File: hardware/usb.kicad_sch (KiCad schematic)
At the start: 6 parts, among them J601 USB_C_Receptacle_USB2.0, U601 SRV05-4

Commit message: work on layout
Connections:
- net USB_M: now also C?.1, U601.3 (IO2); no longer C?.1, U601.1 (IO1)
- net USB_P: now also C?.1, U601.1 (IO1); no longer C?.1, U601.3 (IO2)
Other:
- moved on the sheet: JP601, R601, U601
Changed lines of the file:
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@@
     (company "matei repair lab")
   )
-  (junction (at 170.18 93.98) (diameter 0) (color 0 0 0 0)
-  )
-  (junction (at 190.5 74.93) (diameter 0) (color 0 0 0 0)
+  (junction (at 160.02 88.9) (diameter 0) (color 0 0 0 0)
+  )
+  (junction (at 182.88 74.93) (diameter 0) (color 0 0 0 0)
   )
   (junction (at 149.86 88.9) (diameter 0) (color 0 0 0 0)
@@
   (junction (at 133.35 88.9) (diameter 0) (color 0 0 0 0)
   )
-  (junction (at 190.5 115.57) (diameter 0) (color 0 0 0 0)
+  (junction (at 182.88 115.57) (diameter 0) (color 0 0 0 0)
   )
   (junction (at 133.35 87.63) (diameter 0) (color 0 0 0 0)
@@
   (junction (at 133.35 93.98) (diameter 0) (color 0 0 0 0)
   )
-  (no_connect (at 203.2 93.98))
+  (no_connect (at 195.58 93.98))
   (no_connect (at 129.54 105.41))
-  (no_connect (at 203.2 88.9))
+  (no_connect (at 195.58 88.9))
   (no_connect (at 129.54 102.87))
-  (wire (pts (xy 170.18 86.36) (xy 170.18 93.98))
-    (stroke (width 0) (type default))
-  )
-  (wire (pts (xy 190.5 115.57) (xy 190.5 104.14))
+  (wire (pts (xy 182.88 115.57) (xy 182.88 104.14))
+    (stroke (width 0) (type default))
+  )
+  (wire (pts (xy 160.02 86.36) (xy 160.02 88.9))
     (stroke (width 0) (type default))
   )
@@
     (stroke (width 0) (type default))
   )
-  (wire (pts (xy 190.5 74.93) (xy 190.5 78.74))
-    (stroke (width 0) (type default))
-  )
-  (wire (pts (xy 190.5 115.57) (xy 190.5 118.11))
+  (wire (pts (xy 182.88 74.93) (xy 182.88 78.74))
+    (stroke (width 0) (type default))
+  )
+  (wire (pts (xy 182.88 115.57) (xy 182.88 118.11))
     (stroke (width 0) (type default))
   )
@@
     (stroke (width 0) (type default))
   )
-  (wire (pts (xy 190.5 74.93) (xy 190.5 72.39))
-    (stroke (width 0) (type default))
-  )
-  (wire (pts (xy 170.18 93.98) (xy 177.8 93.98))
+  (wire (pts (xy 182.88 74.93) (xy 182.88 72.39))
     (stroke (width 0) (type default))
   )
@@
     (stroke (width 0) (type default))
   )
-  (wire (pts (xy 114.3 115.57) (xy 190.5 115.57))
-    (stroke (width 0) (type default))
-  )
-  (wire (pts (xy 149.86 88.9) (xy 177.8 88.9))
-    (stroke (width 0) (type default))
-  )
-  (wire (pts (xy 129.54 74.93) (xy 179.07 74.93))
-    (stroke (width 0) (type default))
-  )
-  (wire (pts (xy 186.69 74.93) (xy 190.5 74.93))
+  (wire (pts (xy 114.3 115.57) (xy 182.88 115.57))
+    (stroke (width 0) (type default))
+  )
+  (wire (pts (xy 149.86 88.9) (xy 160.02 88.9))
+    (stroke (width 0) (type default))
+  )
+  (wire (pts (xy 129.54 74.93) (xy 171.45 74.93))
+    (stroke (width 0) (type default))
+  )
+  (wire (pts (xy 179.07 74.93) (xy 182.88 74.93))
+    (stroke (width 0) (type default))
+  )
+  (wire (pts (xy 160.02 88.9) (xy 170.18 88.9))
     (stroke (width 0) (type default))
   )
@@
     (stroke (width 0) (type default))
   )
-  (wire (pts (xy 170.18 78.74) (xy 170.18 81.28))
+  (wire (pts (xy 160.02 78.74) (xy 160.02 81.28))
     (stroke (width 0) (type default))
   )
@@
     (effects (font (size 1.27 1.27)) (justify left bottom))
   )
-  (hierarchical_label "USB_M" (shape bidirectional) (at 135.89 86.36 0) (fields_autoplaced)
+  (hierarchical_label "USB_M" (shape bidirectional) (at 135.89 96.52 0) (fields_autoplaced)
     (effects (font (size 1.27 1.27)) (justify left))
   )
@@
     (effects (font (size 1.27 1.27)) (justify left))
   )
-  (hierarchical_label "USB_P" (shape bidirectional) (at 135.89 96.52 0) (fields_autoplaced)
+  (hierarchical_label "USB_P" (shape bidirectional) (at 135.89 86.36 0) (fields_autoplaced)
     (effects (font (size 1.27 1.27)) (justify left))
   )
@@
     )
   )
-  (symbol (lib_id "Jumper:SolderJumper_2_Bridged") (at 182.88 74.93 0) (unit 1)
+  (symbol (lib_id "Jumper:SolderJumper_2_Bridged") (at 175.26 74.93 0) (unit 1)
     (in_bom yes) (on_board yes) (dnp no) (fields_autoplaced)
-    (property "Reference" "JP601" (at 182.88 68.58 0)
-      (effects (font (size 1.27 1.27)))
-    )
-    (property "Value" "USB5V" (at 182.88 71.12 0)
-      (effects (font (size 1.27 1.27)))
-    )
-    (property "Footprint" "Jumper:SolderJumper-2_P1.3mm_Bridged_RoundedPad1.0x1.5mm" (at 182.88 74.93 0)
-      (effects (font (size 1.27 1.27)) hide)
-    )
-    (property "Datasheet" "~" (at 182.88 74.93 0)
+    (property "Reference" "JP601" (at 175.26 68.58 0)
+      (effects (font (size 1.27 1.27)))
+    )
+    (property "Value" "USB5V" (at 175.26 71.12 0)
+      (effects (font (size 1.27 1.27)))
+    )
+    (property "Footprint" "Jumper:SolderJumper-2_P1.3mm_Bridged_RoundedPad1.0x1.5mm" (at 175.26 74.93 0)
+      (effects (font (size 1.27 1.27)) hide)
+    )
+    (property "Datasheet" "~" (at 175.26 74.93 0)
       (effects (font (size 1.27 1.27)) hide)
     )
@@
     )
   )
-  (symbol (lib_id "Power_Protection:SRV05-4") (at 190.5 91.44 0) (unit 1)
-    (in_bom yes) (on_board yes) (dnp no) (fields_autoplaced)
-    (property "Reference" "U601" (at 193.6497 76.2 0)
+  (symbol (lib_id "Power_Protection:SRV05-4") (at 182.88 91.44 0) (unit 1)
+    (in_bom yes) (on_board yes) (dnp no)
+    (property "Reference" "U601" (at 186.0297 76.2 0)
       (effects (font (size 1.27 1.27)) (justify left))
     )
-    (property "Value" "SRV05-4" (at 193.6497 78.74 0)
+    (property "Value" "SRV05-4" (at 186.0297 78.74 0)
       (effects (font (size 1.27 1.27)) (justify left))
     )
-    (property "Footprint" "Package_TO_SOT_SMD:SOT-23-6" (at 208.28 102.87 0)
-      (effects (font (size 1.27 1.27)) hide)
-    )
-    (property "Datasheet" "http://www.onsemi.com/pub/Collateral/SRV05-4-D.PDF" (at 190.5 91.44 0)
+    (property "Footprint" "Package_TO_SOT_SMD:SOT-23-6" (at 200.66 102.87 0)
+      (effects (font (size 1.27 1.27)) hide)
+    )
+    (property "Datasheet" "http://www.onsemi.com/pub/Collateral/SRV05-4-D.PDF" (at 182.88 91.44 0)
       (effects (font (size 1.27 1.27)) hide)
     )
@@
     )
   )
-  (symbol (lib_id "power:+5V") (at 190.5 72.39 0) (unit 1)
+  (symbol (lib_id "power:+5V") (at 182.88 72.39 0) (unit 1)
     (in_bom yes) (on_board yes) (dnp no) (fields_autoplaced)
-    (property "Reference" "#PWR0603" (at 190.5 76.2 0)
-      (effects (font (size 1.27 1.27)) hide)
-    )
-    (property "Value" "+5V" (at 190.5 67.31 0)
-      (effects (font (size 1.27 1.27)))
-    )
-    (property "Footprint" "" (at 190.5 72.39 0)
-      (effects (font (size 1.27 1.27)) hide)
-    )
-    (property "Datasheet" "" (at 190.5 72.39 0)
+    (property "Reference" "#PWR0603" (at 182.88 76.2 0)
+      (effects (font (size 1.27 1.27)) hide)
+    )
+    (property "Value" "+5V" (at 182.88 67.31 0)
+      (effects (font (size 1.27 1.27)))
+    )
+    (property "Footprint" "" (at 182.88 72.39 0)
+      (effects (font (size 1.27 1.27)) hide)
+    )
+    (property "Datasheet" "" (at 182.88 72.39 0)
       (effects (font (size 1.27 1.27)) hide)
     )
@@
     )
   )
-  (symbol (lib_id "power:+3V3") (at 170.18 78.74 0) (unit 1)
+  (symbol (lib_id "power:+3V3") (at 160.02 78.74 0) (unit 1)
     (in_bom yes) (on_board yes) (dnp no)
-    (property "Reference" "#PWR0601" (at 170.18 82.55 0)
-      (effects (font (size 1.27 1.27)) hide)
-    )
-    (property "Value" "+3V3" (at 175.26 77.47 0)
-      (effects (font (size 1.27 1.27)))
-    )
-    (property "Footprint" "" (at 170.18 78.74 0)
-      (effects (font (size 1.27 1.27)) hide)
-    )
-    (property "Datasheet" "" (at 170.18 78.74 0)
+    (property "Reference" "#PWR0601" (at 160.02 82.55 0)
+      (effects (font (size 1.27 1.27)) hide)
+    )
+    (property "Value" "+3V3" (at 165.1 77.47 0)
+      (effects (font (size 1.27 1.27)))
+    )
+    (property "Footprint" "" (at 160.02 78.74 0)
+      (effects (font (size 1.27 1.27)) hide)
+    )
+    (property "Datasheet" "" (at 160.02 78.74 0)
       (effects (font (size 1.27 1.27)) hide)
     )
@@
     )
   )
-  (symbol (lib_id "Device:R_Small_US") (at 170.18 83.82 0) (unit 1)
+  (symbol (lib_id "Device:R_Small_US") (at 160.02 83.82 0) (unit 1)
     (in_bom yes) (on_board yes) (dnp no) (fields_autoplaced)
-    (property "Reference" "R601" (at 172.72 82.55 0)
+    (property "Reference" "R601" (at 162.56 82.55 0)
       (effects (font (size 1.27 1.27)) (justify left))
     )
-    (property "Value" "1.5k" (at 172.72 85.09 0)
+    (property "Value" "1.5k" (at 162.56 85.09 0)
       (effects (font (size 1.27 1.27)) (justify left))
     )
-    (property "Footprint" "Resistor_SMD:R_0402_1005Metric" (at 170.18 83.82 0)
-      (effects (font (size 1.27 1.27)) hide)
-    )
-    (property "Datasheet" "~" (at 170.18 83.82 0)
+    (property "Footprint" "Resistor_SMD:R_0402_1005Metric" (at 160.02 83.82 0)
+      (effects (font (size 1.27 1.27)) hide)
+    )
+    (property "Datasheet" "~" (at 160.02 83.82 0)
       (effects (font (size 1.27 1.27)) hide)
     )
@@
     )
   )
-  (symbol (lib_id "power:GND") (at 190.5 118.11 0) (unit 1)
+  (symbol (lib_id "power:GND") (at 182.88 118.11 0) (unit 1)
     (in_bom yes) (on_board yes) (dnp no) (fields_autoplaced)
-    (property "Reference" "#PWR0604" (at 190.5 124.46 0)
-      (effects (font (size 1.27 1.27)) hide)
-    )
-    (property "Value" "GND" (at 190.5 123.19 0)
-      (effects (font (size 1.27 1.27)))
-    )
-    (property "Footprint" "" (at 190.5 118.11 0)
-      (effects (font (size 1.27 1.27)) hide)
-    )
-    (property "Datasheet" "" (at 190.5 118.11 0)
-      (effects (font (size 1.27 1.27)) hide)
-    )
+    (property "Reference" "#PWR0604" (at 182.88 124.46 0)
+      (effects (font (size 1.27 1.27)) hide)
+    )
+    (property "Value" "GND" (at 182.88 123.19 0)
+      (effects (font (size 1.27 1.27)))
+    )
+    (property "Footprint" "" (at 182.88 118.11 0)
+      (effects (font (size 1.27 1.27)) hide)
+    )
+    (property "Datasheet" "" (at 182.88 118.11 0)
+      (effects (font (size 1.27 1.27)) hide)
+    )

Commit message: finalize fab files
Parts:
- R601: now not fitted; now left out of the parts list
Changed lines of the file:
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@@
   )
   (symbol (lib_id "Device:R_Small_US") (at 160.02 83.82 0) (unit 1)
-    (in_bom yes) (on_board yes) (dnp no) (fields_autoplaced)
+    (in_bom no) (on_board yes) (dnp yes) (fields_autoplaced)
     (property "Reference" "R601" (at 162.56 82.55 0)
       (effects (font (size 1.27 1.27)) (justify left))

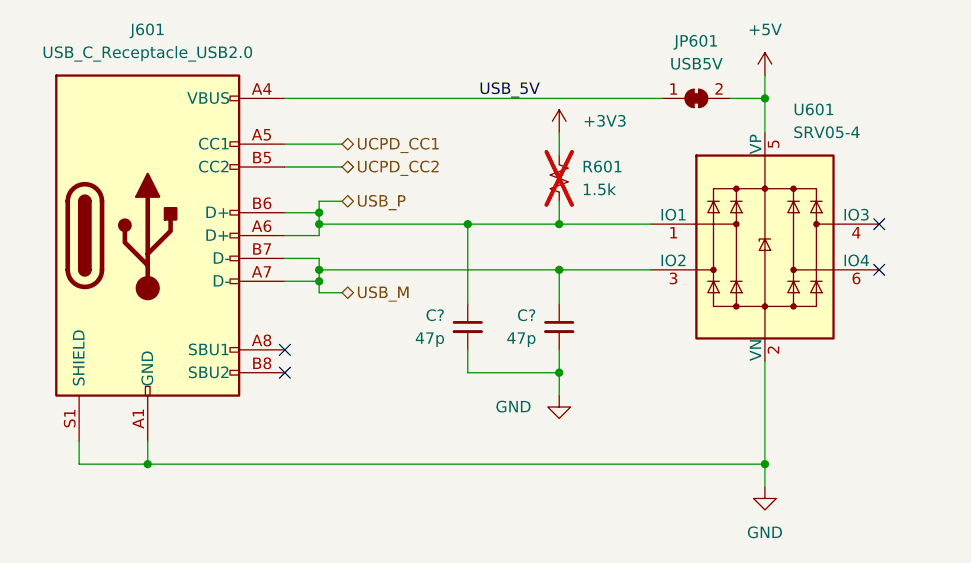
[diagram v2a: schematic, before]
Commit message: update schematic (Vref+ tie to Vdd) and go through ERC check
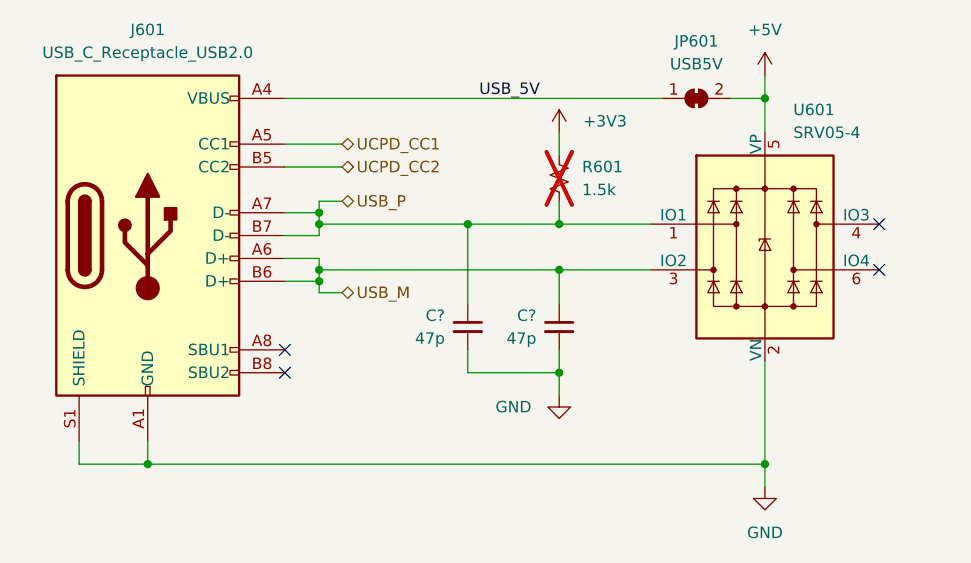
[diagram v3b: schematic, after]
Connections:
- net USB_M: now also J601.A6 (D+), J601.B6 (D+); no longer J601.A7 (D-), J601.B7 (D-)
- net USB_P: now also J601.A7 (D-), J601.B7 (D-); no longer J601.A6 (D+), J601.B6 (D+)

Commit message: Fix swapped USB pins
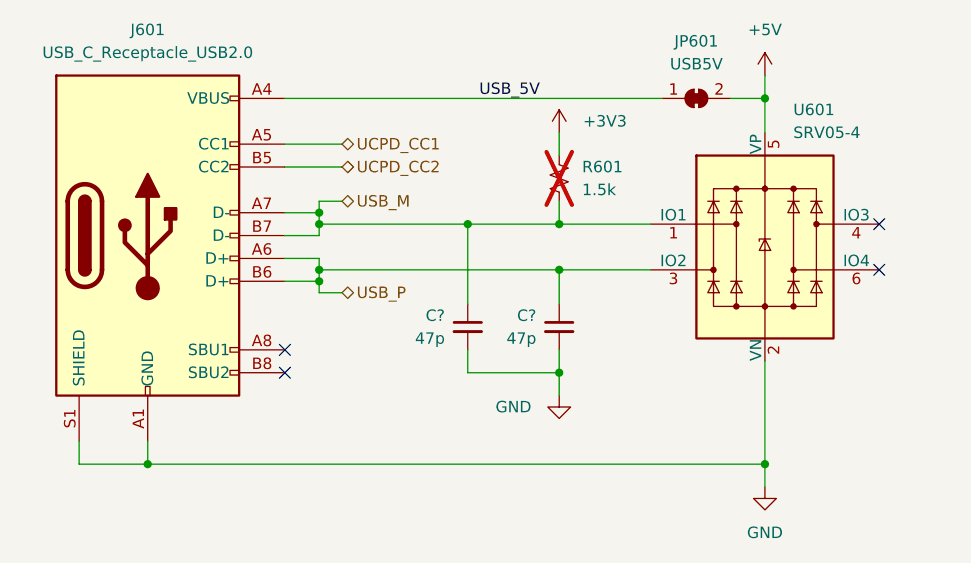
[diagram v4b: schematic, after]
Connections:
- net USB_M: now also C?.1, J601.A7 (D-), J601.B7 (D-), R601.2, U601.1 (IO1); no longer C?.1, J601.A6 (D+), J601.B6 (D+), U601.3 (IO2)
- net USB_P: now also C?.1, J601.A6 (D+), J601.B6 (D+), U601.3 (IO2); no longer C?.1, J601.A7 (D-), J601.B7 (D-), R601.2, U601.1 (IO1)
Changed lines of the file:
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@@
     (effects (font (size 1.27 1.27)) (justify left bottom))
   )
-  (hierarchical_label "USB_M" (shape bidirectional) (at 135.89 96.52 0) (fields_autoplaced)
+  (hierarchical_label "USB_M" (shape bidirectional) (at 135.89 86.36 0) (fields_autoplaced)
     (effects (font (size 1.27 1.27)) (justify left))
   )
@@
     (effects (font (size 1.27 1.27)) (justify left))
   )
-  (hierarchical_label "USB_P" (shape bidirectional) (at 135.89 86.36 0) (fields_autoplaced)
+  (hierarchical_label "USB_P" (shape bidirectional) (at 135.89 96.52 0) (fields_autoplaced)
     (effects (font (size 1.27 1.27)) (justify left))
   )

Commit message: update schematic to remove debounce cap
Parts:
- JP601: now left out of the parts list
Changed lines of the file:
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@@
   )
   (symbol (lib_id "Jumper:SolderJumper_2_Bridged") (at 175.26 74.93 0) (unit 1)
-    (in_bom yes) (on_board yes) (dnp no) (fields_autoplaced)
+    (in_bom no) (on_board yes) (dnp no) (fields_autoplaced)
     (property "Reference" "JP601" (at 175.26 68.58 0)
       (effects (font (size 1.27 1.27)))
